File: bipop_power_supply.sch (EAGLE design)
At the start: 22 parts, among them IC1 LM1117MP-3.3, IC2 LM1117MP-5.0, X2 MSTBA6

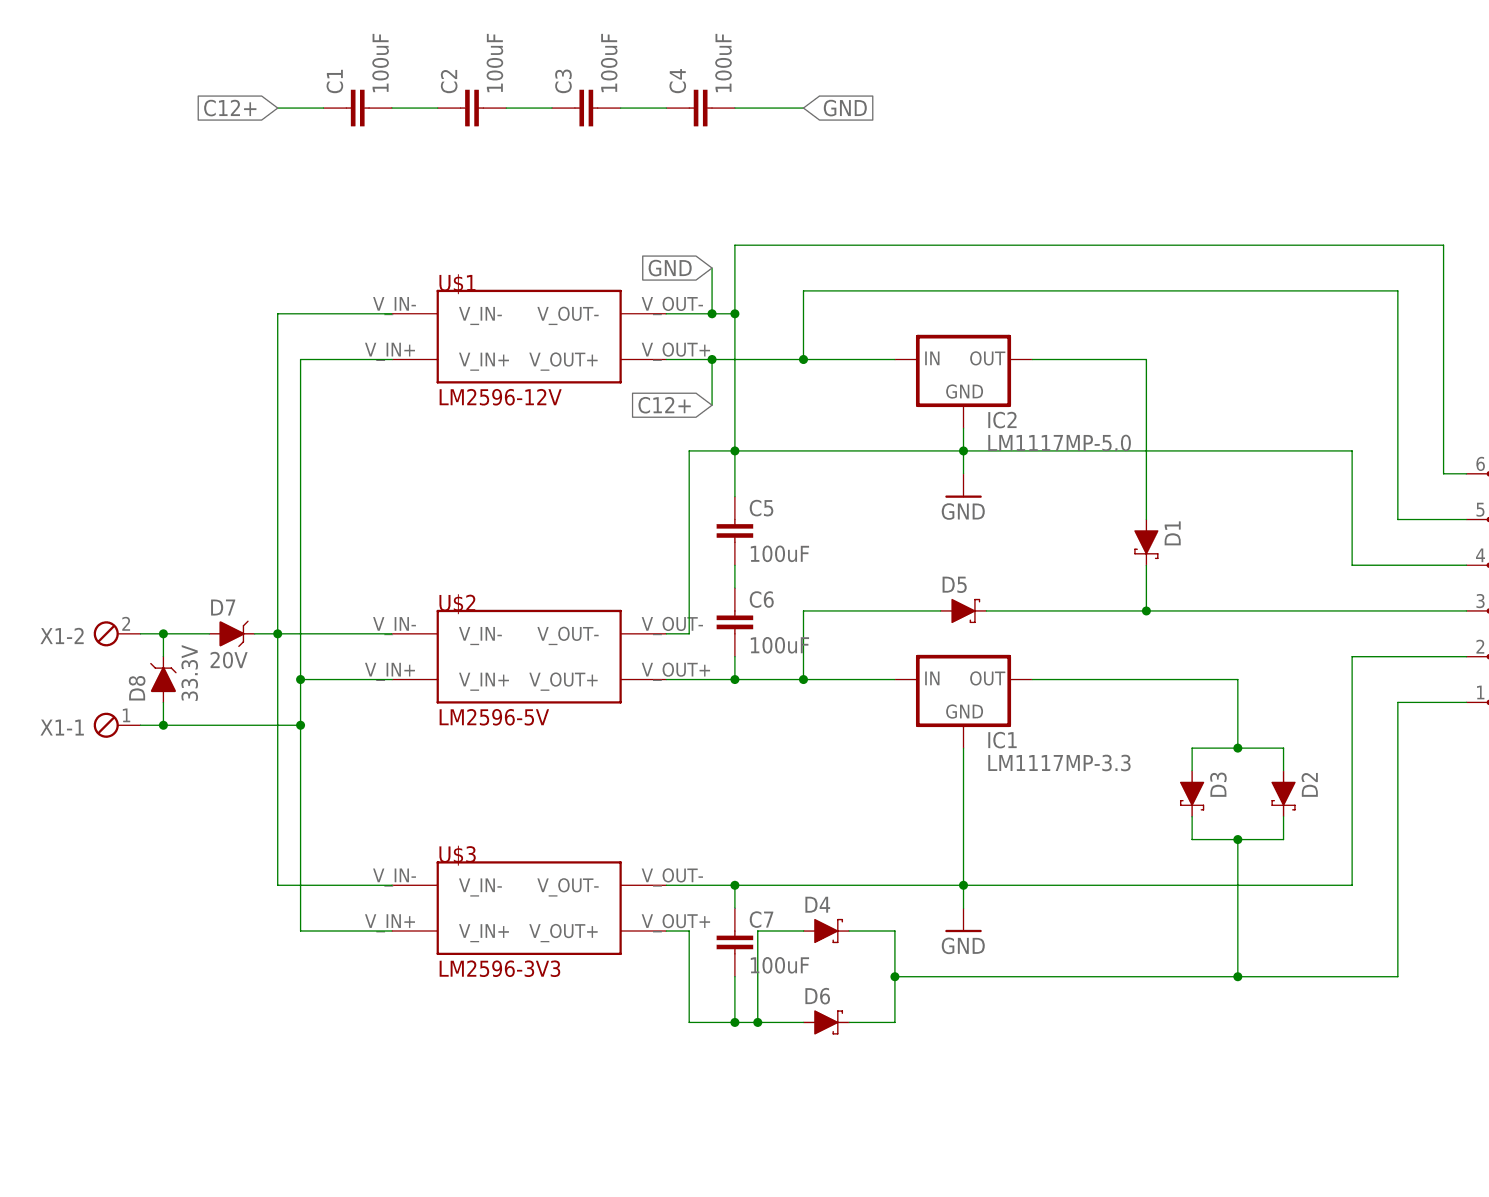
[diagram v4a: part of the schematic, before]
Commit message: Fixed polarisation in power_supply board.
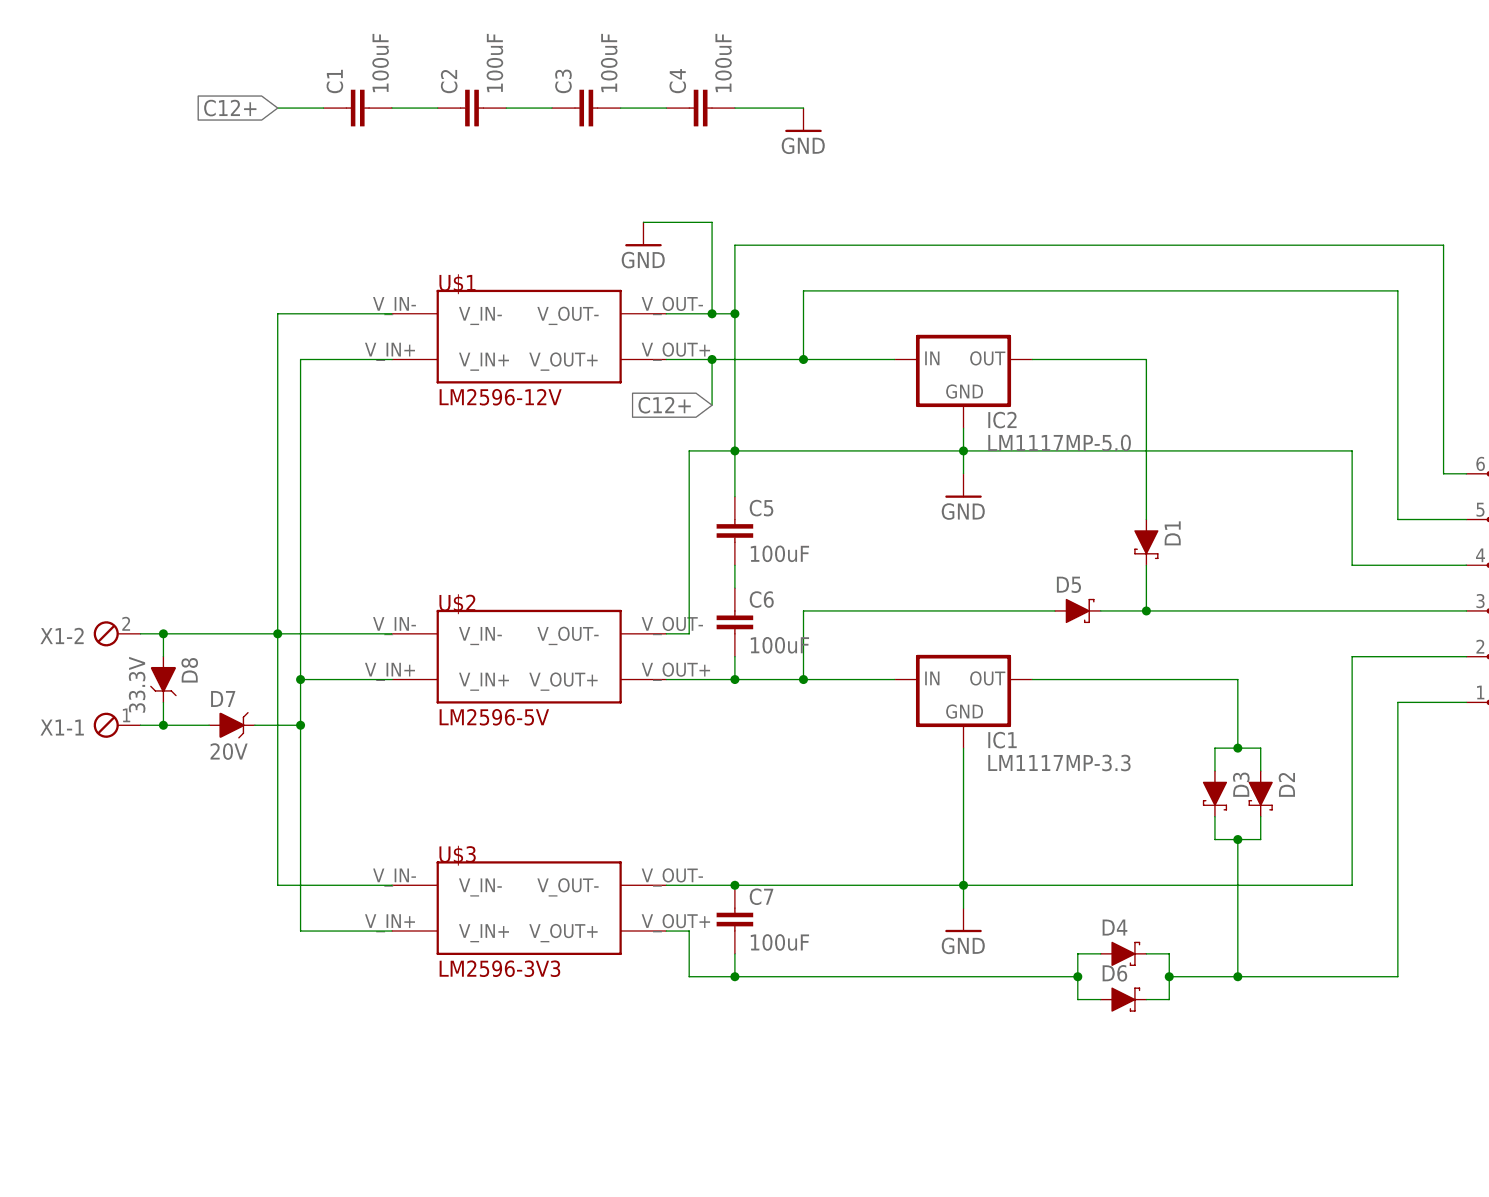
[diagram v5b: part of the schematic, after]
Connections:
- removed net N$17: D7.C, U$1.V_IN-, U$2.V_IN-, U$3.V_IN-
- new net N$10: D7.A, D8.C, X1-1.1
- net N$1: now also D8.A, U$1.V_IN-, U$2.V_IN-, U$3.V_IN-; no longer D7.A, D8.C
- net N$22: now also D7.C; no longer D8.A, X1-1.1
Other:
- moved on the sheet: C7, D2, D3, D4, D5, D6, D7, D8

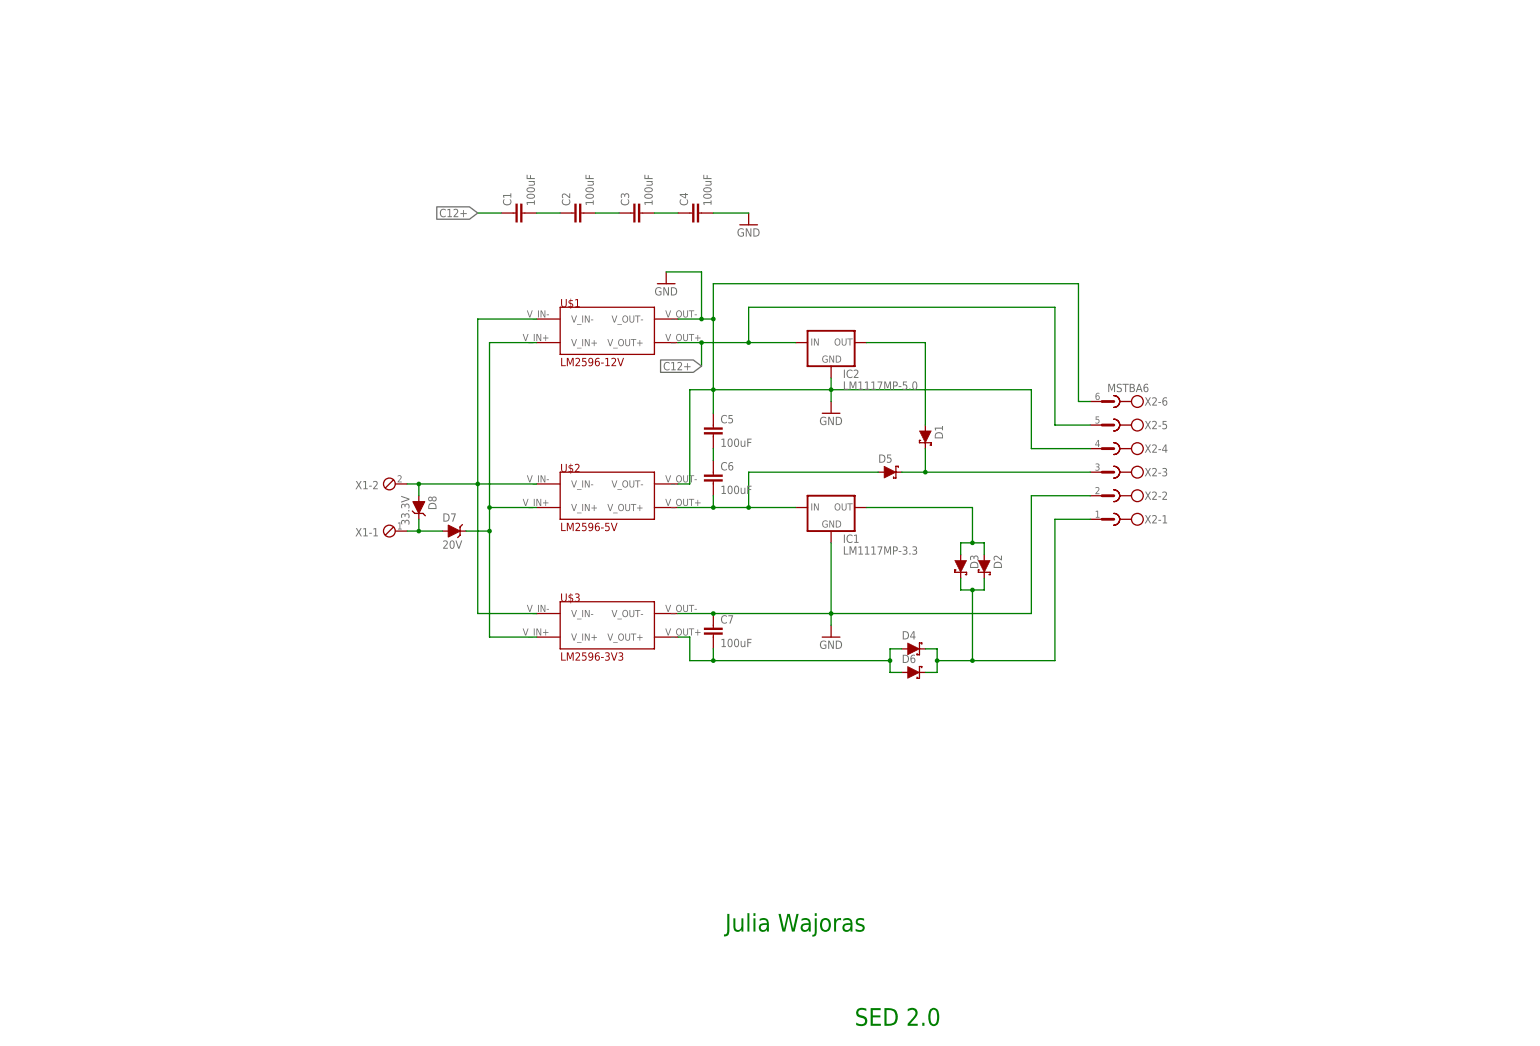
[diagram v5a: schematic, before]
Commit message: added current sensors to power supply, NO ADC yet
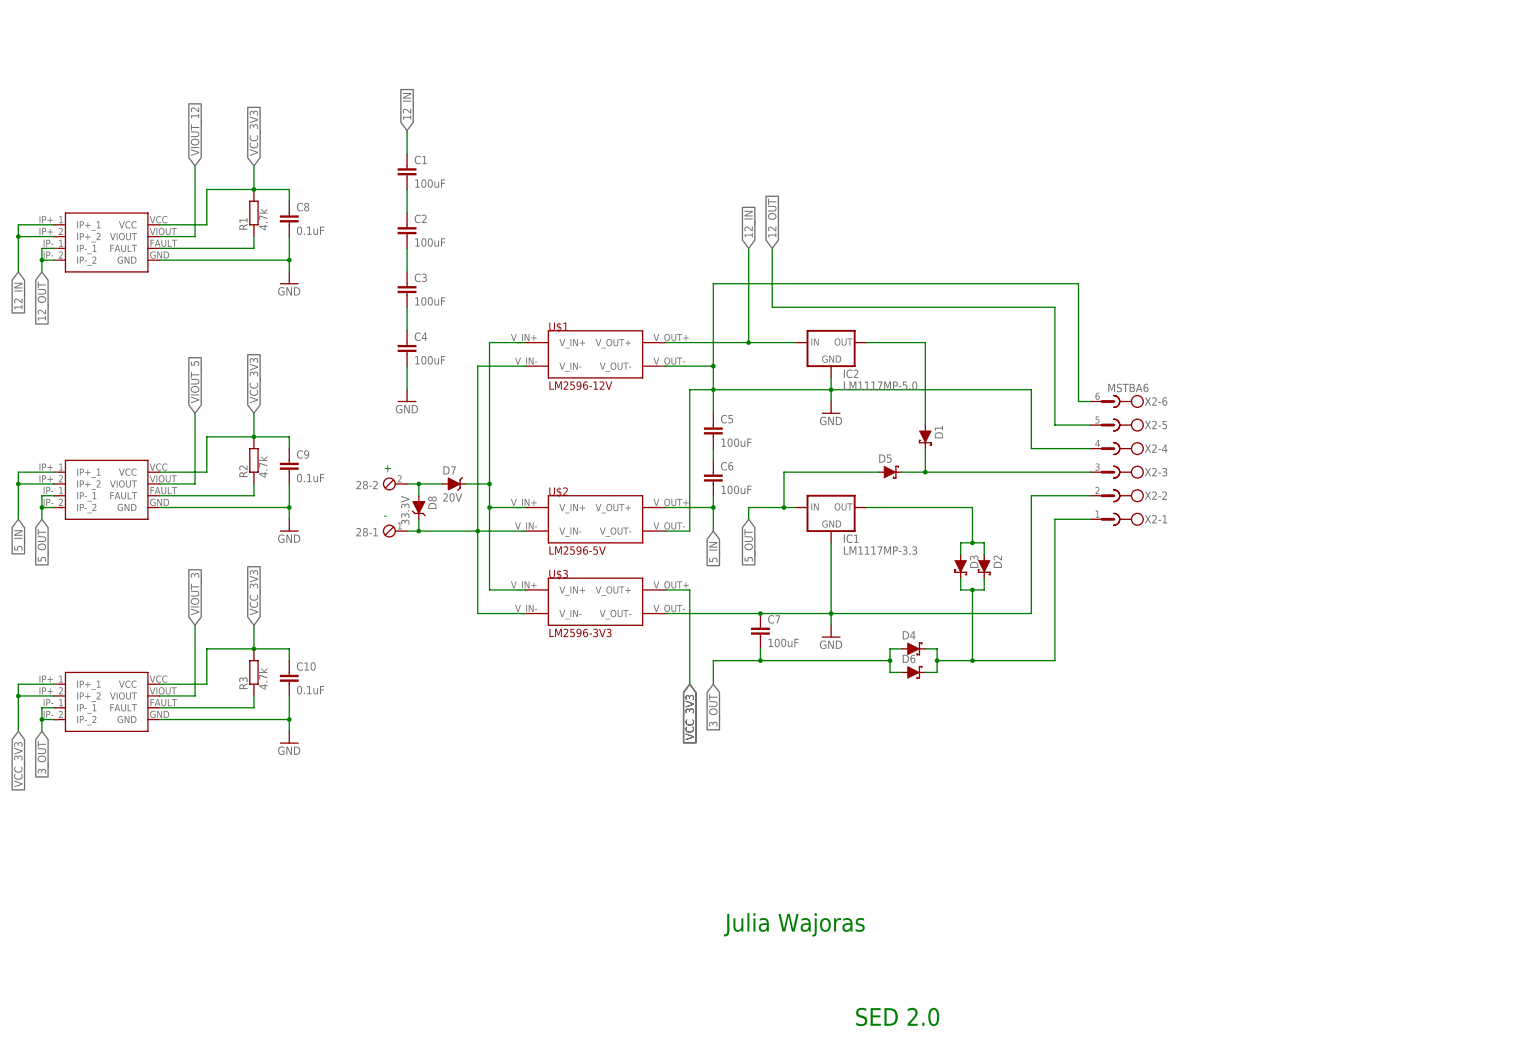
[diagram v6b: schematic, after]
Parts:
- added C10, C8, C9: 0.1uF, rcl:C-EUC0805
- added R1, R2, R3: 4.7k, resistor-shunt:BVS
- added U$5, U$6, U$7: ACS711, lustro_pcb:ACS711
- renumbered X1 to 28
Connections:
- removed net C12+: C1.1, IC2.IN, U$1.V_OUT+, X2-5.1
- removed net N$22: D7.C, U$1.V_IN+, U$2.V_IN+, U$3.V_IN+
- removed net N$7: C7.2, D4.A, D6.A, U$3.V_OUT+
- new net 12_IN: C1.1, IC2.IN, U$1.V_OUT+, U$5.IP+_1, U$5.IP+_2
- new net 12_OUT: U$5.IP-_1, U$5.IP-_2, X2-5.1
- new net 3_OUT: C7.2, D4.A, D6.A, U$7.IP-_1, U$7.IP-_2
- new net 5_IN: C6.2, U$2.V_OUT+, U$6.IP+_1, U$6.IP+_2
- new net 5_OUT: D5.A, IC1.IN, U$6.IP-_1, U$6.IP-_2
- new net N$12: 28-2.1, D7.A, D8.A
- new net N$13: R2.2, U$6.FAULT
- new net N$14: U$3.V_OUT+
- new net VCC_3V3: C10.1, C8.1, C9.1, D7.C, R1.1, R2.1, R3.1, U$1.V_IN+, U$2.V_IN+, U$3.V_IN+, U$5.VCC, U$6.VCC, U$7.IP+_1, U$7.IP+_2, U$7.VCC
- new net VIOUT_12: U$5.VIOUT
- new net VIOUT_3: U$7.VIOUT
- new net VIOUT_5: U$6.VIOUT
- net GND: now also C10.2, C8.2, C9.2, U$5.GND, U$6.GND, U$7.GND
- net N$1: now also R1.2, U$5.FAULT; no longer 28-2.1, D8.A, U$1.V_IN-, U$2.V_IN-, U$3.V_IN-
- net N$10: now also U$1.V_IN-, U$2.V_IN-, U$3.V_IN-; no longer D7.A
- net N$4: now also R3.2, U$7.FAULT; no longer C6.2, D5.A, IC1.IN, U$2.V_OUT+
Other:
- note added: "+"
- note added: "-"
- moved on the sheet: C1, C2, C3, C4, C7, D7, U$1, U$2, U$3

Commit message: pin interface for current sensors added
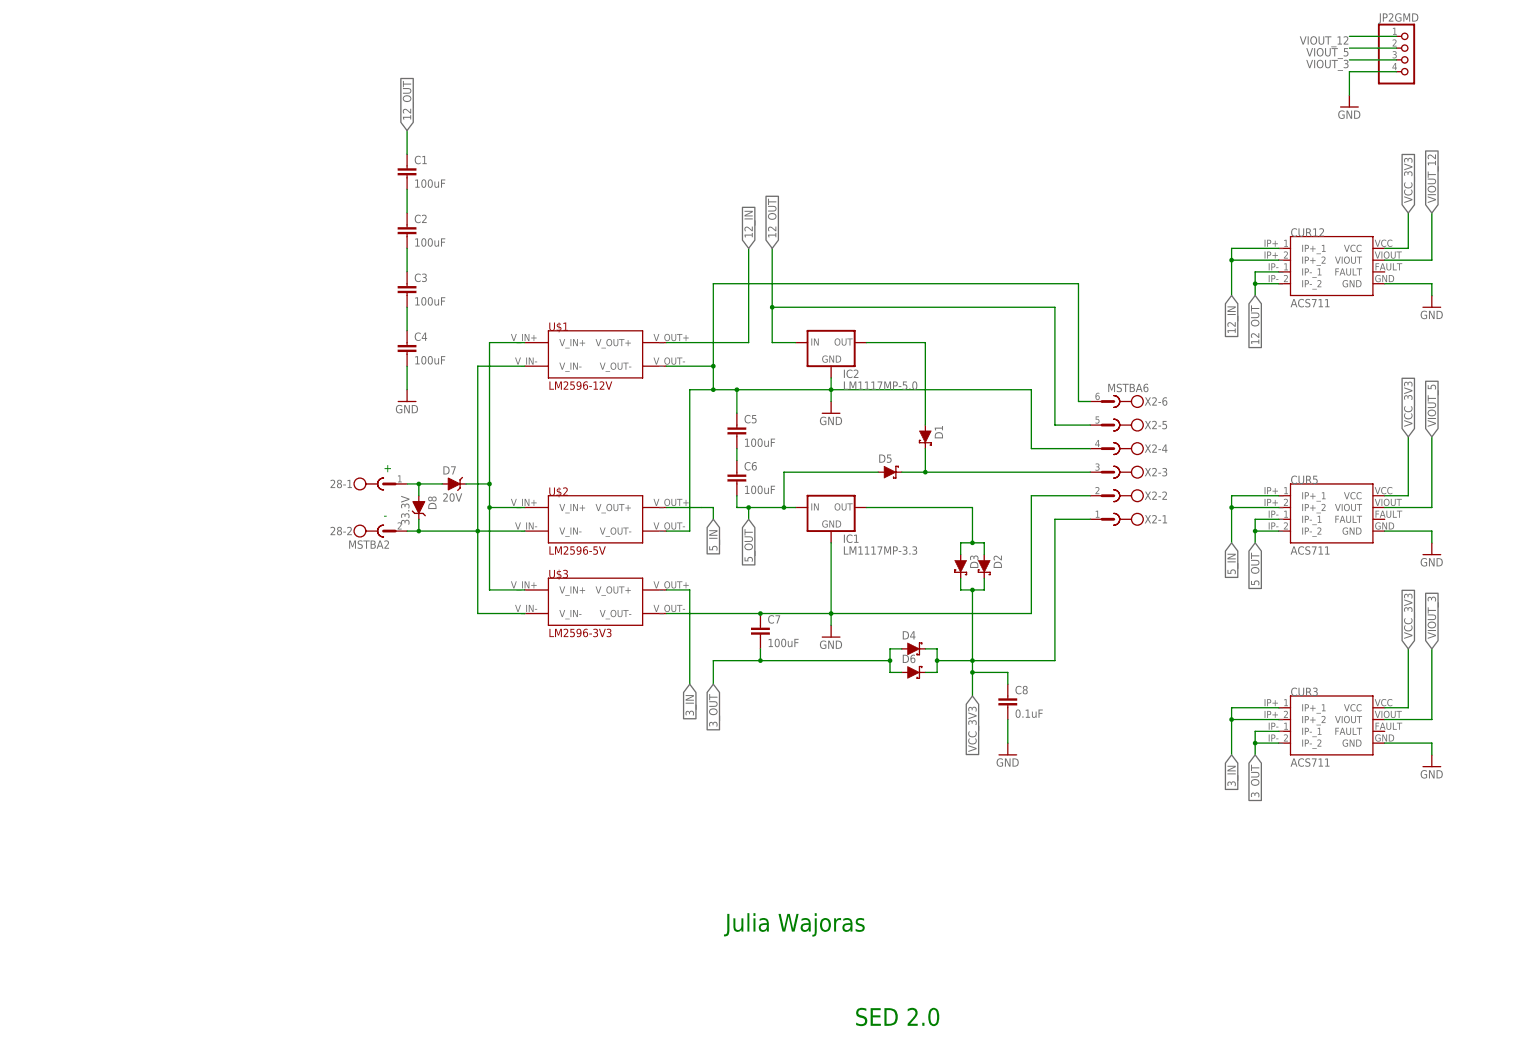
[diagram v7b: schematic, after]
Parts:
- removed C10, C9: 0.1uF, rcl:C-EUC0805
- removed R1, R2, R3: 4.7k, resistor-shunt:BVS
- removed U$5, U$6, U$7: ACS711, lustro_pcb:ACS711
- added CUR12, CUR3, CUR5: ACS711, lustro_pcb:ACS711
- added JP2GMD: (no value), pinhead:PINHD-1X4
- 28: value (none) -> MSTBA2; device con-phoenix-254:MPT2 -> con-phoenix-508:MSTBA2
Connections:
- removed net N$1: R1.2, U$5.FAULT
- removed net N$11: D2.C, D3.C, D4.C, D6.C, X2-1.1
- removed net N$13: R2.2, U$6.FAULT
- removed net N$14: U$3.V_OUT+
- removed net N$4: R3.2, U$7.FAULT
- new net 3_IN: CUR3.IP+_1, CUR3.IP+_2, U$3.V_OUT+
- new net MM: D7.C, U$1.V_IN+, U$2.V_IN+, U$3.V_IN+
- net 12_IN: now also CUR12.IP+_1, CUR12.IP+_2; no longer C1.1, IC2.IN, U$5.IP+_1, U$5.IP+_2
- net 12_OUT: now also C1.1, CUR12.IP-_1, CUR12.IP-_2, IC2.IN; no longer U$5.IP-_1, U$5.IP-_2
- net 3_OUT: now also CUR3.IP-_1, CUR3.IP-_2; no longer U$7.IP-_1, U$7.IP-_2
- net 5_IN: now also CUR5.IP+_1, CUR5.IP+_2; no longer C6.2, U$6.IP+_1, U$6.IP+_2
- net 5_OUT: now also C6.2, CUR5.IP-_1, CUR5.IP-_2; no longer U$6.IP-_1, U$6.IP-_2
- net GND: now also CUR12.GND, CUR3.GND, CUR5.GND, JP2GMD.4; no longer C10.2, C9.2, U$5.GND, U$6.GND, U$7.GND
- net N$10: now also 28-2.1; no longer 28-1.1
- net N$12: now also 28-1.1; no longer 28-2.1
- net VCC_3V3: now also CUR12.VCC, CUR3.VCC, CUR5.VCC, D2.C, D3.C, D4.C, D6.C, X2-1.1; no longer C10.1, C9.1, D7.C, R1.1, R2.1, R3.1, U$1.V_IN+, U$2.V_IN+, U$3.V_IN+, U$5.VCC, U$6.VCC, U$7.IP+_1, U$7.IP+_2, U$7.VCC
- net VIOUT_12: now also CUR12.VIOUT, JP2GMD.1; no longer U$5.VIOUT
- net VIOUT_3: now also CUR3.VIOUT, JP2GMD.3; no longer U$7.VIOUT
- net VIOUT_5: now also CUR5.VIOUT, JP2GMD.2; no longer U$6.VIOUT
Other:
- moved on the sheet: C5, C6, C8
